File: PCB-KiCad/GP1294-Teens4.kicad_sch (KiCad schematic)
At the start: 26 parts, among them U8 CS8421

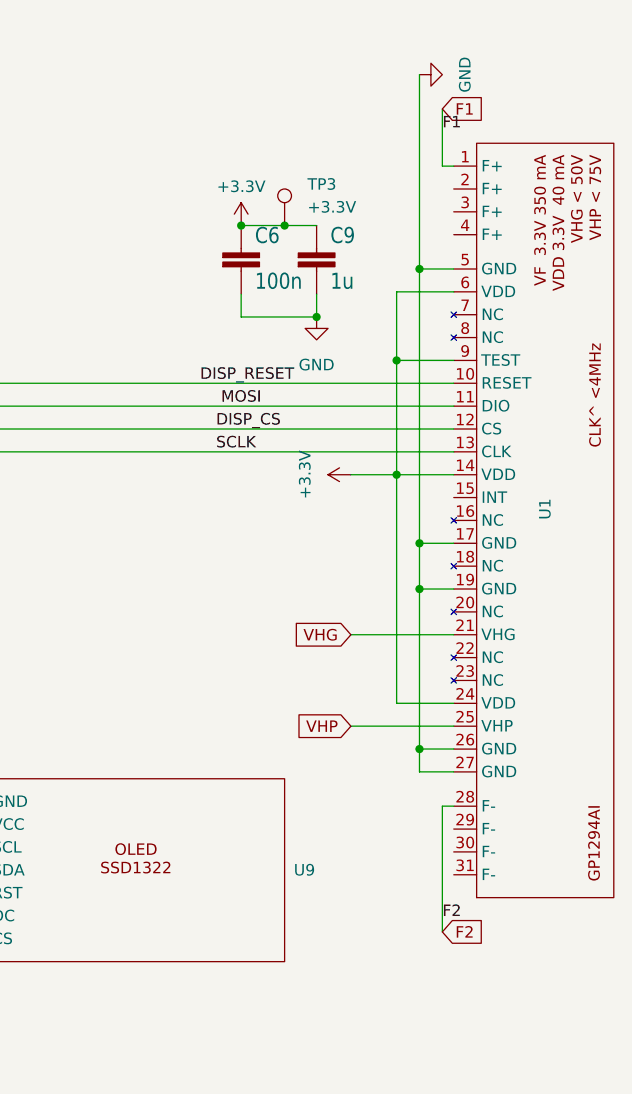
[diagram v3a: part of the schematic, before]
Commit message: PCB: TestPin must pull up with 100k.
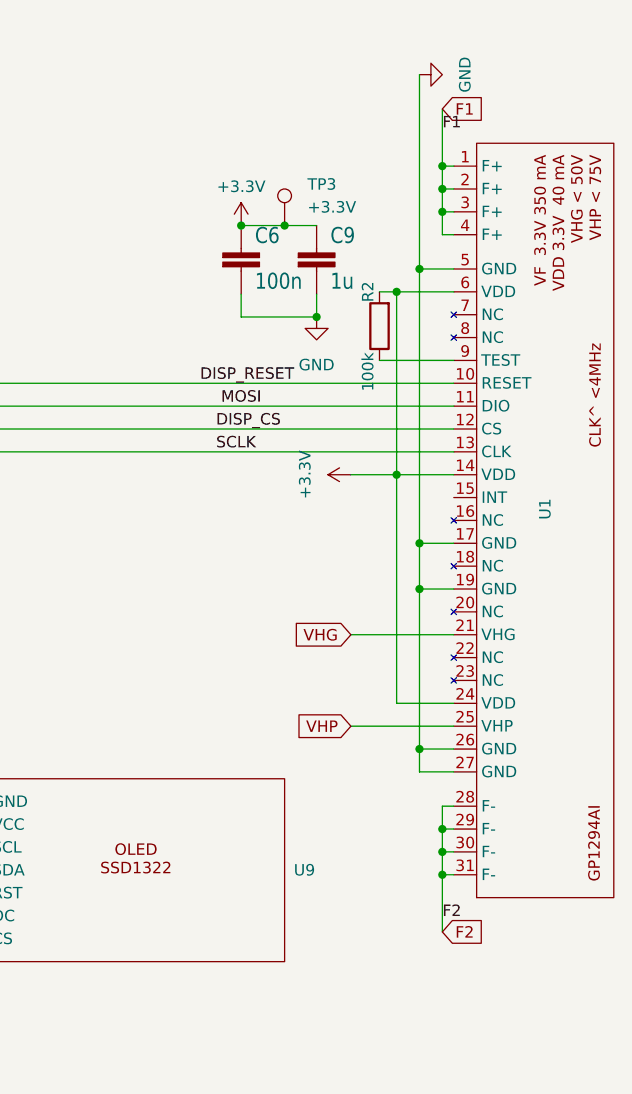
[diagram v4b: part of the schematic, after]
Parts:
- added R2: 100k, Resistor_SMD:R_0603_1608Metric, symbol Device:R
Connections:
- net +3.3V: now also R2.2; no longer U1.9 (TEST)
- net F1: now also U1.2 (F+), U1.3 (F+), U1.4 (F+)
- net F2: now also U1.29 (F-), U1.30 (F-), U1.31 (F-)
- new net: R2.1, U1.9 (TEST)
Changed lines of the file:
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@@
   (junction (at 153.67 161.29) (diameter 0) (color 0 0 0 0)
   )
+  (junction (at 248.92 132.08) (diameter 0) (color 0 0 0 0)
+  )
   (junction (at 179.832 120.904) (diameter 0) (color 0 0 0 0)
   )
   (junction (at 115.57 186.69) (diameter 0) (color 0 0 0 0)
   )
-  (junction (at 243.84 74.93) (diameter 0) (color 0 0 0 0)
-  )
   (junction (at 153.67 173.99) (diameter 0) (color 0 0 0 0)
   )
   (junction (at 231.394 59.944) (diameter 0) (color 0 0 0 0)
   )
+  (junction (at 248.92 129.54) (diameter 0) (color 0 0 0 0)
+  )
   (junction (at 246.38 64.77) (diameter 0) (color 0 0 0 0)
   )
@@
   (junction (at 115.57 168.91) (diameter 0) (color 0 0 0 0)
   )
+  (junction (at 248.92 58.42) (diameter 0) (color 0 0 0 0)
+  )
   (junction (at 184.15 113.03) (diameter 0) (color 0 0 0 0)
   )
@@
   (junction (at 234.95 70.104) (diameter 0) (color 0 0 0 0)
   )
+  (junction (at 248.92 127) (diameter 0) (color 0 0 0 0)
+  )
   (junction (at 153.67 163.83) (diameter 0) (color 0 0 0 0)
   )
   (junction (at 173.736 35.052) (diameter 0) (color 0 0 0 0)
   )
+  (junction (at 243.84 67.31) (diameter 0) (color 0 0 0 0)
+  )
+  (junction (at 248.92 55.88) (diameter 0) (color 0 0 0 0)
+  )
   (junction (at 153.67 158.75) (diameter 0) (color 0 0 0 0)
   )
@@
   (junction (at 246.38 118.11) (diameter 0) (color 0 0 0 0)
   )
+  (junction (at 248.92 53.34) (diameter 0) (color 0 0 0 0)
+  )
+  (wire (pts (xy 250.19 58.42) (xy 248.92 58.42))
+    (stroke (width 0) (type default))
+  )
   (wire (pts (xy 181.61 118.11) (xy 181.61 80.01))
     (stroke (width 0) (type default))
@@
     (stroke (width 0) (type default))
   )
+  (wire (pts (xy 248.92 127) (xy 250.19 127))
+    (stroke (width 0) (type default))
+  )
   (wire (pts (xy 127.762 35.052) (xy 173.736 35.052))
     (stroke (width 0) (type default))
   )
   (wire (pts (xy 246.38 95.25) (xy 246.38 100.33))
+    (stroke (width 0) (type default))
+  )
+  (wire (pts (xy 248.92 127) (xy 248.92 129.54))
     (stroke (width 0) (type default))
   )
@@
     (stroke (width 0) (type default))
   )
-  (wire (pts (xy 248.92 124.46) (xy 248.92 138.43))
+  (wire (pts (xy 248.92 124.46) (xy 248.92 127))
     (stroke (width 0) (type default))
   )
@@
     (stroke (width 0) (type default))
   )
+  (wire (pts (xy 250.19 60.96) (xy 248.92 60.96))
+    (stroke (width 0) (type default))
+  )
   (wire (pts (xy 186.436 113.03) (xy 184.15 113.03))
     (stroke (width 0) (type default))
@@
     (stroke (width 0) (type default))
   )
-  (wire (pts (xy 243.84 74.93) (xy 250.19 74.93))
-    (stroke (width 0) (type default))
-  )
   (wire (pts (xy 246.38 64.77) (xy 250.19 64.77))
     (stroke (width 0) (type default))
@@
     (stroke (width 0) (type default))
   )
+  (wire (pts (xy 248.92 129.54) (xy 250.19 129.54))
+    (stroke (width 0) (type default))
+  )
+  (wire (pts (xy 248.92 129.54) (xy 248.92 132.08))
+    (stroke (width 0) (type default))
+  )
   (wire (pts (xy 195.834 136.652) (xy 127.254 136.652))
     (stroke (width 0) (type default))
@@
   )
   (wire (pts (xy 195.834 134.112) (xy 180.086 134.112))
-    (stroke (width 0) (type default))
-  )
-  (wire (pts (xy 243.84 87.63) (xy 243.84 74.93))
     (stroke (width 0) (type default))
   )
@@
     (stroke (width 0) (type default))
   )
+  (wire (pts (xy 248.92 55.88) (xy 248.92 58.42))
+    (stroke (width 0) (type default))
+  )
+  (wire (pts (xy 248.92 132.08) (xy 248.92 138.43))
+    (stroke (width 0) (type default))
+  )
   (wire (pts (xy 243.84 113.03) (xy 250.19 113.03))
     (stroke (width 0) (type default))
@@
     (stroke (width 0) (type default))
   )
+  (wire (pts (xy 241.935 67.31) (xy 243.84 67.31))
+    (stroke (width 0) (type default))
+  )
   (wire (pts (xy 158.75 105.41) (xy 172.72 105.41))
     (stroke (width 0) (type default))
@@
     (stroke (width 0) (type default))
   )
-  (wire (pts (xy 243.84 74.93) (xy 243.84 67.31))
+  (wire (pts (xy 243.84 67.31) (xy 243.84 87.63))
     (stroke (width 0) (type default))
   )
@@
   )
   (wire (pts (xy 114.3 168.91) (xy 115.57 168.91))
+    (stroke (width 0) (type default))
+  )
+  (wire (pts (xy 248.92 132.08) (xy 250.19 132.08))
     (stroke (width 0) (type default))
   )
@@
   )
   (wire (pts (xy 153.67 163.83) (xy 153.67 166.37))
+    (stroke (width 0) (type default))
+  )
+  (wire (pts (xy 248.92 53.34) (xy 248.92 55.88))
+    (stroke (width 0) (type default))
+  )
+  (wire (pts (xy 250.19 55.88) (xy 248.92 55.88))
+    (stroke (width 0) (type default))
+  )
+  (wire (pts (xy 241.935 74.93) (xy 250.19 74.93))
+    (stroke (width 0) (type default))
+  )
+  (wire (pts (xy 248.92 58.42) (xy 248.92 60.96))
     (stroke (width 0) (type default))
   )
@@
         (path "/3de011e3-f89b-42a8-8637-1f4c3f0867fa"
           (reference "C6") (unit 1)
+        )
+      )
+    )
+  )
+  (symbol (lib_id "Device:R") (at 241.935 71.12 180) (unit 1)
+    (in_bom yes) (on_board yes) (dnp no)
+    (property "Reference" "R2" (at 240.665 67.31 90)
+      (effects (font (size 1.27 1.27)))
+    )
+    (property "Value" "100k" (at 240.665 76.2 90)
+      (effects (font (size 1.27 1.27)))
+    )
+    (property "Footprint" "Resistor_SMD:R_0603_1608Metric" (at 243.713 71.12 90)
+      (effects (font (size 1.27 1.27)) hide)
+    )
+    (property "Datasheet" "~" (at 241.935 71.12 0)
+      (effects (font (size 1.27 1.27)) hide)
+    )
+    (property "Field4" "" (at 241.935 71.12 90)
+      (effects (font (size 1.27 1.27)) hide)
+    )
+    (pin "1")
+    (pin "2")
+    (instances
+      (project "GP1294-Teens4"
+        (path "/3de011e3-f89b-42a8-8637-1f4c3f0867fa"
+          (reference "R2") (unit 1)
         )
       )
@@
     )
     (pin "1")
+    (pin "2")
+    (pin "3")
     (pin "4")
     (pin "5")
+    (pin "6")
     (pin "7")
-    (pin "6")
-    (pin "2")
-    (pin "3")
     (instances
       (project "GP1294-Teens4"
@@
       (effects (font (size 1.27 1.27)) hide)
     )
-    (pin "9")
+    (pin "1")
+    (pin "10")
+    (pin "11")
     (pin "2")
     (pin "3")
     (pin "4")
-    (pin "11")
-    (pin "8")
     (pin "5")
     (pin "6")
-    (pin "10")
-    (pin "1")
     (pin "7")
-    (instances
-      (project "GP1294-Teens4"
+    (pin "8")
+    (pin "9")
+    (instances
+      (project "GP1294-Teens4"
